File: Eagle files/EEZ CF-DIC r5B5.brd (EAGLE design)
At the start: 155 x 90 mm, 260 parts, among them IC1 VIPer35L, IC2 SI8233BB-D-IS1, IC3 LM5041B, IC4 LM258D, IC5 IR11688STRPBF, IC6 LM258D, IC7 TL103W, P1 T910W-50K, Q1 MMBT5551, Q2 C3M0280090D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

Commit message: C4, C5, C17 value changed
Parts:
- C17, C4, C5: value CY1Y-470P -> CY1Y-4N7
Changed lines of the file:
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@@
 <attribute name="VALUE" x="144.4959" y="52.5341" size="1.016" layer="27" ratio="10"/>
 </element>
-<element name="C5" library="EEZ_Lib1" package="CY075-032X103" value="CY1Y-470P" x="115.1255" y="77.216" smashed="yes">
+<element name="C5" library="EEZ_Lib1" package="CY075-032X103" value="CY1Y-4N7" x="115.1255" y="77.216" smashed="yes">
 <attribute name="NAME" x="114.1817" y="78.9299" size="1.27" layer="25" ratio="10"/>
 <attribute name="VALUE" x="111.0615" y="76.454" size="1.016" layer="27" ratio="10"/>
 </element>
-<element name="C4" library="EEZ_Lib1" package="CY075-032X103" value="CY1Y-470P" x="115.1255" y="72.3265" smashed="yes">
+<element name="C4" library="EEZ_Lib1" package="CY075-032X103" value="CY1Y-4N7" x="115.1255" y="72.3265" smashed="yes">
 <attribute name="NAME" x="114.2365" y="74.168" size="1.27" layer="25" ratio="10"/>
 <attribute name="VALUE" x="111.0615" y="71.5645" size="1.016" layer="27" ratio="10"/>
@@
 <attribute name="VALUE" x="97.282" y="58.547" size="1.016" layer="28" ratio="10" rot="MR180"/>
 </element>
-<element name="C17" library="EEZ_Lib1" package="CY075-032X103" value="CY1Y-470P" x="119.507" y="42.926" smashed="yes" rot="R270">
+<element name="C17" library="EEZ_Lib1" package="CY075-032X103" value="CY1Y-4N7" x="119.507" y="42.926" smashed="yes" rot="R270">
 <attribute name="NAME" x="117.602" y="43.1165" size="1.27" layer="25" ratio="10" rot="R90"/>
 <attribute name="VALUE" x="118.745" y="46.99" size="1.016" layer="27" ratio="10" rot="R270"/>

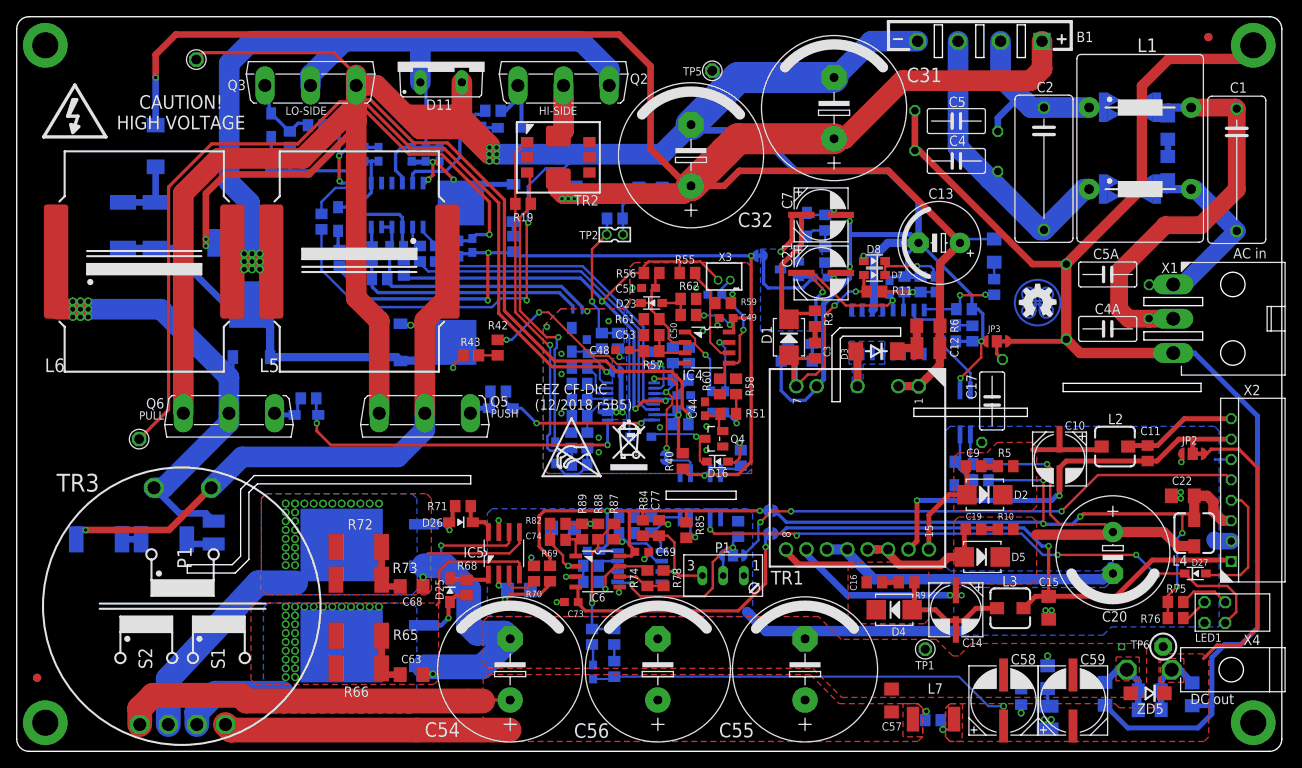
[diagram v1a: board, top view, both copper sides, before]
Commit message: Mechanical drawings, optional EMI parts
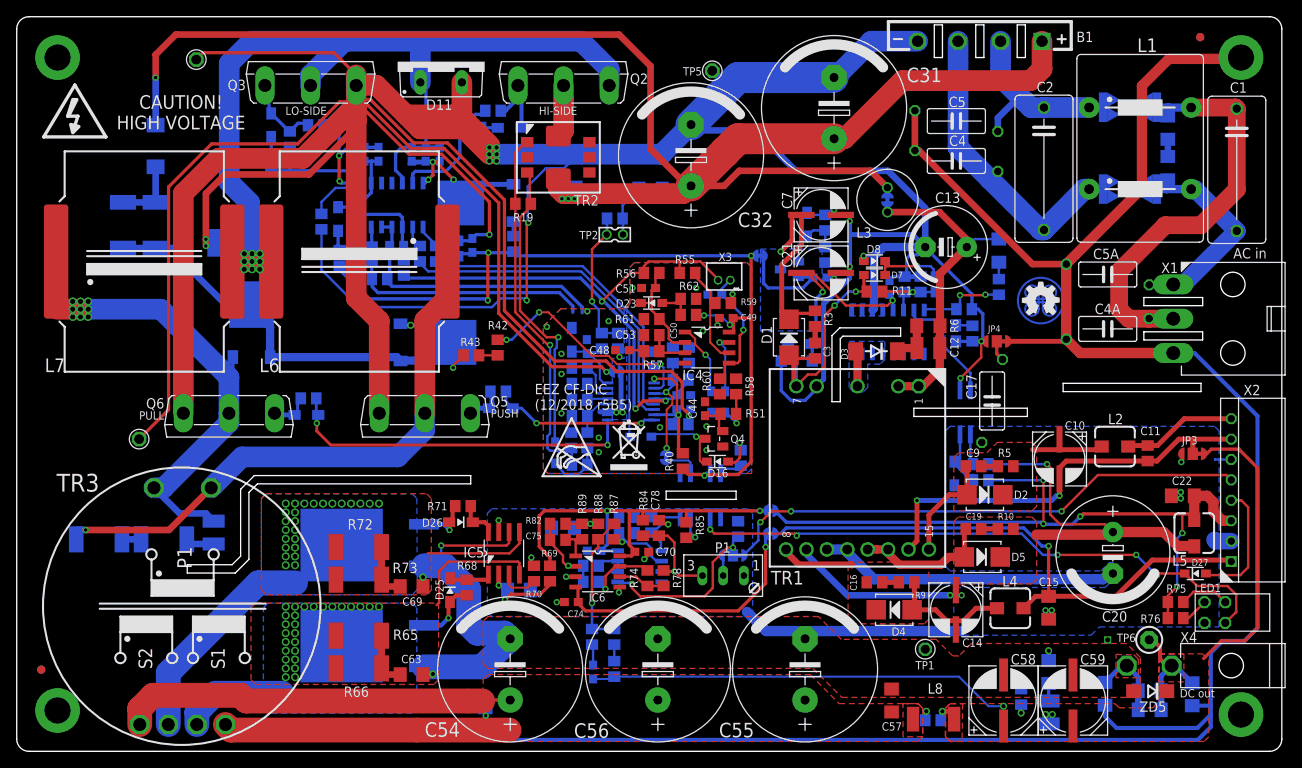
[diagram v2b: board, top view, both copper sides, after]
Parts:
- added C79: N.C., rcl:C0805
- added JP9: JP2-NOCUT, EEZ_Lib1:JP2-NOCUT
- added L8: IHLP2020CZER3R3M11, EEZ_inductors_and_transformers:IHLP-2020BZ-11
- C69: value 100n -> 4n7/200V; device rcl:C0603 -> rcl:C1206
- C70: value 10n -> 100n
- C71: value 100n -> 10n
- C72, C74: value 100p -> 100n; device rcl:C0805 -> rcl:C0603
- C73: value 100n -> 100p; device rcl:C0603 -> rcl:C0805
- C75: value 2n2 -> 100p
- C76: value 4u7 -> 2n2; device EEZ_Lib1:EC1206 -> rcl:C0805
- C77: value 1u -> 4u7; device rcl:C0805 -> EEZ_Lib1:EC1206
- C78: value N.C. -> 1u
- JP2, JP7: value JP3-CUT -> JP2-NOCUT; device EEZ_Lib1:JP3-CUT -> EEZ_Lib1:JP2-NOCUT
- JP4, JP8: value JP2-NOCUT -> JP3-CUT; device EEZ_Lib1:JP2-NOCUT -> EEZ_Lib1:JP3-CUT
- L3: value DLG-0403-180 -> RLB0812-471KL; device EEZ_inductors_and_transformers:DE0403 -> EEZ_Lib1:FERSYTER_DSZ6
- L5: value 60B684C -> DLG-0403-180; device EEZ_inductors_and_transformers:MURATA_6000B -> EEZ_inductors_and_transformers:DE0403
- L7: value IHLP2020CZER3R3M11 -> 60B684C; device EEZ_inductors_and_transformers:IHLP-2020BZ-11 -> EEZ_inductors_and_transformers:MURATA_6000B
- moved L7 111.8 mm to (15.6, 60.0), turned to 0 degrees
- moved L5 107.6 mm to (144.3, 26.7)
- moved C66 86.7 mm to (57.4, 3.94)
- moved C68 86.0 mm to (133.3, 7.05), flipped to the bottom, turned to 270 degrees
- moved L3 52.3 mm to (106.7, 67.6), turned to 270 degrees
- moved JP2 48.7 mm to (106.7, 67.6), flipped to the bottom, turned to 270 degrees
- moved JP4 46.8 mm to (120.1, 50.2), flipped to the top, turned to 180 degrees
- moved C69 28.5 mm to (48.4, 20.2)
- moved JP3 27.7 mm to (144.1, 36.4)
- moved L6 26.4 mm to (42.0, 60.0), turned to 180 degrees
- moved JP5 25.5 mm to (73.5, 46.5)
- moved L4 24.4 mm to (121.7, 17.5), turned to 90 degrees
- moved C70 15.9 mm to (76.6, 24.4), flipped to the top, turned to 0 degrees
- moved C71 14.9 mm to (70.6, 9.72), turned to 90 degrees
- moved JP8 14.5 mm to (87.8, 24.0), turned to 0 degrees
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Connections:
- new net VIPER+: C12.1, C13.+, JP2.2, L3.P$2, R6.1, R7.1, TR1.1, TR1.2
- net +2.5VREF: now also C78.1; no longer C77.1
- net +6V_REC: now also L5.1; no longer L4.1
- net -15V: now also JP3.COM; no longer JP2.COM
- net -7V_REC: now also L4.1; no longer L3.1
- net 0V: now also JP4.NO, JP5.2; no longer JP3.NO, JP4.2
- net AGND: now also JP5.1; no longer JP4.1
- net BUCK_OUT: now also L7.2; no longer L5.2
- net COMP: now also JP9.1; no longer JP8.1
- net DC_BUS: now also JP2.1, L3.P$1; no longer C12.1, C13.+, R6.1, R7.1, TR1.1, TR1.2
- net GND: now also C68.1, C70.2, C72.2, C74.2, C77.-, C79.2, JP3.NO; no longer C67.1, C68.2, C71.2, C73.2, C76.-, C77.2, JP2.NO
- net L_PULL: now also L7.1; no longer L6.1
- net L_PUSH: now also L6.1; no longer L5.1
- net N$10: now also C73.2; no longer C72.2
- net N$134: now also C75.1; no longer C74.1
- net N$28: now also C71.2; no longer C70.2
- net N$39: now also C74.1, JP7.1; no longer C73.1, JP6.1
- net N$4: now also JP4.COM; no longer JP3.COM
- net N$44: now also JP9.2; no longer JP8.2
- net N$46: now also C70.1, C72.1, JP6.2; no longer C69.1, C71.1, JP5.2
- net N$57: now also C79.1, JP8.COM; no longer C78.1, JP7.COM
- net N$58: now also JP8.NO; no longer JP7.NO
- net N$64: now also C75.2; no longer C74.2
- net N$67: now also C69.1; no longer C68.1
- net N$76: now also C73.1, C76.1; no longer C72.1, C75.1
- net N$9: now also C76.2; no longer C75.2
- net NFB_OFFSET: now also C77.+; no longer C76.+
- net PE: now also C68.2, JP4.NC; no longer JP3.NC
- net POUT+: now also C66.1, L8.1; no longer L7.1
- net PREG_OUT+: now also C67.1, C71.1, JP3.NC, L8.2; no longer C66.1, C70.1, JP2.NC, L7.2
- net U_MON: now also JP8.NC; no longer JP7.NC
- net V+: now also JP6.1, L5.2; no longer JP5.1, L4.2
- net V-: now also JP7.2, L4.2; no longer JP6.2, L3.2
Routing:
- net PE: track 172.4 -> 262.8 mm
- net VIPER+: track 0.00 -> 39.5 mm
- net DC_BUS: track 232.1 -> 194.9 mm
- net PREG_OUT+: track 102.5 -> 107.5 mm
- net 0V: track 676.0 -> 677.9 mm
- net POUT+: track 18.0 -> 18.9 mm, vias 1 -> 2
- net GND: track 161.1 -> 161.8 mm
- net N$20: track 10.3 -> 10.9 mm

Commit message: C46 increased to 2n2 (Eagle files)
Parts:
- C46: value 470p -> 2n2
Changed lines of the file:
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@@
 <setting verticaltext="up"/>
 </settings>
-<grid distance="0.5" unitdist="mm" unit="mm" style="lines" multiple="10" display="no" altdistance="2.5" altunitdist="mil" altunit="mil"/>
+<grid distance="2.5" unitdist="mil" unit="mil" style="lines" multiple="10" display="no" altdistance="2.5" altunitdist="mil" altunit="mil"/>
 <layers>
-<layer number="1" name="Top" color="3" fill="1" visible="yes" active="yes"/>
+<layer number="1" name="Top" color="3" fill="1" visible="no" active="yes"/>
 <layer number="2" name="Route2" color="1" fill="3" visible="no" active="no"/>
 <layer number="3" name="Route3" color="4" fill="3" visible="no" active="no"/>
@@
 <layer number="14" name="Route14" color="1" fill="6" visible="no" active="no"/>
 <layer number="15" name="Route15" color="4" fill="6" visible="no" active="no"/>
-<layer number="16" name="Bottom" color="1" fill="1" visible="yes" active="yes"/>
-<layer number="17" name="Pads" color="14" fill="1" visible="yes" active="yes"/>
-<layer number="18" name="Vias" color="6" fill="1" visible="yes" active="yes"/>
-<layer number="19" name="Unrouted" color="6" fill="1" visible="yes" active="yes"/>
+<layer number="16" name="Bottom" color="1" fill="1" visible="no" active="yes"/>
+<layer number="17" name="Pads" color="14" fill="1" visible="no" active="yes"/>
+<layer number="18" name="Vias" color="6" fill="1" visible="no" active="yes"/>
+<layer number="19" name="Unrouted" color="6" fill="1" visible="no" active="yes"/>
 <layer number="20" name="Dimension" color="4" fill="1" visible="yes" active="yes"/>
-<layer number="21" name="tPlace" color="7" fill="1" visible="yes" active="yes"/>
+<layer number="21" name="tPlace" color="7" fill="1" visible="no" active="yes"/>
 <layer number="22" name="bPlace" color="6" fill="1" visible="yes" active="yes"/>
-<layer number="23" name="tOrigins" color="15" fill="1" visible="yes" active="yes"/>
-<layer number="24" name="bOrigins" color="15" fill="1" visible="yes" active="yes"/>
-<layer number="25" name="tNames" color="7" fill="1" visible="yes" active="yes"/>
+<layer number="23" name="tOrigins" color="15" fill="1" visible="no" active="yes"/>
+<layer number="24" name="bOrigins" color="15" fill="1" visible="no" active="yes"/>
+<layer number="25" name="tNames" color="7" fill="1" visible="no" active="yes"/>
 <layer number="26" name="bNames" color="5" fill="1" visible="yes" active="yes"/>
 <layer number="27" name="tValues" color="12" fill="1" visible="no" active="yes"/>
-<layer number="28" name="bValues" color="10" fill="1" visible="no" active="yes"/>
+<layer number="28" name="bValues" color="10" fill="1" visible="yes" active="yes"/>
 <layer number="29" name="tStop" color="7" fill="1" visible="no" active="yes"/>
-<layer number="30" name="bStop" color="7" fill="1" visible="no" active="yes"/>
+<layer number="30" name="bStop" color="7" fill="1" visible="yes" active="yes"/>
 <layer number="31" name="tCream" color="7" fill="4" visible="no" active="yes"/>
 <layer number="32" name="bCream" color="7" fill="5" visible="no" active="yes"/>
@@
 <layer number="37" name="tTest" color="7" fill="1" visible="no" active="yes"/>
 <layer number="38" name="bTest" color="7" fill="1" visible="no" active="yes"/>
-<layer number="39" name="tKeepout" color="15" fill="1" visible="yes" active="yes"/>
+<layer number="39" name="tKeepout" color="15" fill="1" visible="no" active="yes"/>
 <layer number="40" name="bKeepout" color="5" fill="1" visible="yes" active="yes"/>
 <layer number="41" name="tRestrict" color="14" fill="10" visible="no" active="yes"/>
@@
 </element>
 <element name="C45" library="rcl" package="C0603" value="100n" x="81.7245" y="43.6245" smashed="yes" rot="MR0">
-<attribute name="NAME" x="79.121" y="42.545" size="0.8128" layer="26" ratio="10" rot="MR90"/>
+<attribute name="NAME" x="79.121" y="42.3545" size="0.8128" layer="26" ratio="10" rot="MR90"/>
 <attribute name="VALUE" x="79.9465" y="44.196" size="1.016" layer="28" ratio="10" rot="MR180"/>
 </element>
@@
 <attribute name="VALUE" x="69.2785" y="37.084" size="1.016" layer="28" ratio="10" rot="MR90"/>
 </element>
-<element name="C46" library="rcl" package="C0805" value="470p" x="68.961" y="41.0845" smashed="yes" rot="MR180">
+<element name="C46" library="rcl" package="C0805" value="2n2" x="68.961" y="41.0845" smashed="yes" rot="MR180">
 <attribute name="NAME" x="66.802" y="40.767" size="1.016" layer="26" ratio="10" rot="MR0"/>
-<attribute name="VALUE" x="67.945" y="41.5925" size="1.016" layer="28" ratio="10" rot="MR180"/>
+<attribute name="VALUE" x="67.437" y="41.5925" size="1.016" layer="28" ratio="10" rot="MR180"/>
 </element>
 <element name="R32" library="rcl" package="R0805" value="47K" x="36.6395" y="76.708" smashed="yes" rot="MR180">
